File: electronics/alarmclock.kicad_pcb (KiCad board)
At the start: 2 copper layers, 16 parts, among them J1 SWD, J2 AudioJack2, J3 Conn_02x08_Top_Bottom, J4 SocketTop, J5 SocketBottom, J6 PinheaderTop, J7 PinheaderBottom, SW1 Reset, SW2 Rotary_Encoder_Switch, U1 STM32L011K4T6

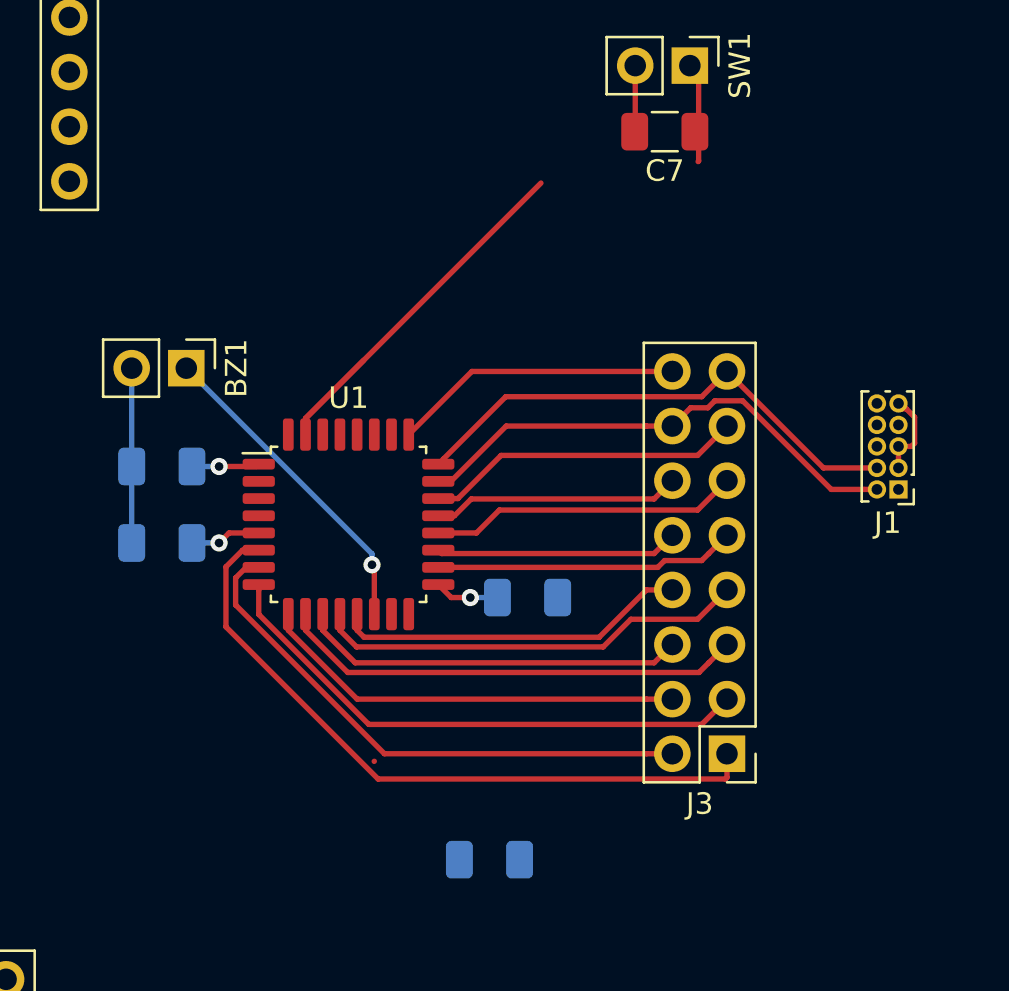
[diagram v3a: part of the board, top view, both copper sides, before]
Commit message: yet another microcontroller switch. added shiftregisters, added battery backup
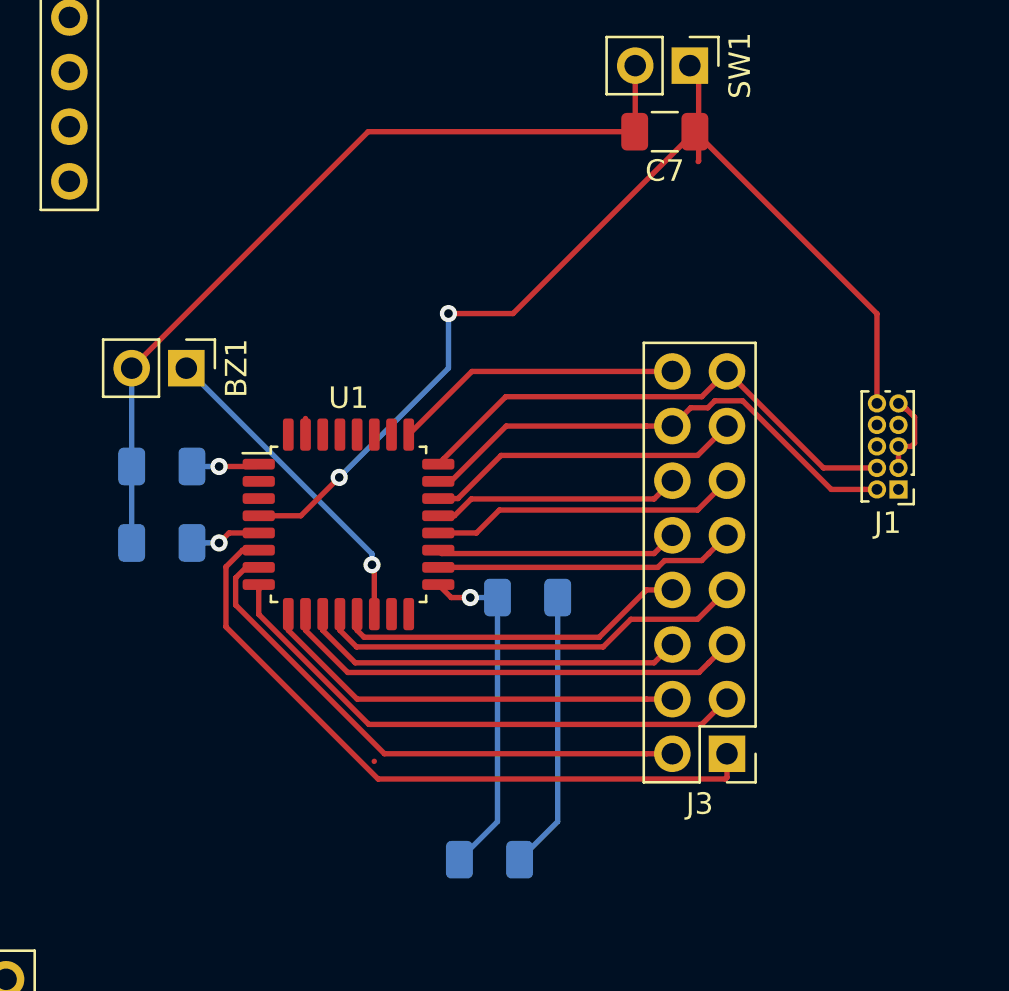
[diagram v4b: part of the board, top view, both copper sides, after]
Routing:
- net NRST: track 4.64 -> 50.0 mm, vias 0 -> 2
- net GND: track 15.3 -> 56.1 mm
- net Switch_Encoder: track 20.1 -> 0.75 mm
- net +3V3: track 9.46 -> 22.4 mm
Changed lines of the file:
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@@
     (thickness 1.6)
     (drawings 0)
-    (tracks 132)
+    (tracks 146)
     (zones 0)
     (modules 16)
@@
       (effects (font (size 1 1) (thickness 0.15)))
     )
-    (fp_text user %R (at 0 8.89 90) (layer F.Fab)
-      (effects (font (size 1 1) (thickness 0.15)))
-    )
     (fp_line (start -1.27 -1.27) (end 0.635 -1.27) (layer F.Fab) (width 0.1))
     (fp_line (start 0.635 -1.27) (end 1.27 -0.635) (layer F.Fab) (width 0.1))
@@
     (fp_line (start 1.75 19.55) (end -1.8 19.55) (layer F.CrtYd) (width 0.05))
     (fp_line (start -1.8 19.55) (end -1.8 -1.8) (layer F.CrtYd) (width 0.05))
+    (fp_text user %R (at 0 8.89 90) (layer F.Fab)
+      (effects (font (size 1 1) (thickness 0.15)))
+    )
     (pad 8 thru_hole oval (at 0 17.78) (size 1.7 1.7) (drill 1) (layers *.Cu *.Mask)
       (net 23 "Net-(J4-Pad8)"))
@@
       (effects (font (size 1 1) (thickness 0.15)))
     )
-    (fp_text user %R (at 0 8.89 90) (layer F.Fab)
-      (effects (font (size 1 1) (thickness 0.15)))
-    )
     (fp_line (start -1.8 19.55) (end -1.8 -1.8) (layer F.CrtYd) (width 0.05))
     (fp_line (start 1.75 19.55) (end -1.8 19.55) (layer F.CrtYd) (width 0.05))
@@
     (fp_line (start 0.635 -1.27) (end 1.27 -0.635) (layer F.Fab) (width 0.1))
     (fp_line (start -1.27 -1.27) (end 0.635 -1.27) (layer F.Fab) (width 0.1))
+    (fp_text user %R (at 0 8.89 90) (layer F.Fab)
+      (effects (font (size 1 1) (thickness 0.15)))
+    )
     (pad 1 thru_hole rect (at 0 0) (size 1.7 1.7) (drill 1) (layers *.Cu *.Mask)
       (net 31 "Net-(J5-Pad1)"))
@@
       (effects (font (size 1 1) (thickness 0.15)))
     )
-    (fp_text user %R (at 0 8.89 90) (layer F.Fab)
-      (effects (font (size 1 1) (thickness 0.15)))
-    )
     (fp_line (start 1.8 -1.8) (end -1.8 -1.8) (layer F.CrtYd) (width 0.05))
     (fp_line (start 1.8 19.55) (end 1.8 -1.8) (layer F.CrtYd) (width 0.05))
@@
     (fp_line (start 1.27 -1.27) (end 1.27 19.05) (layer F.Fab) (width 0.1))
     (fp_line (start -0.635 -1.27) (end 1.27 -1.27) (layer F.Fab) (width 0.1))
+    (fp_text user %R (at 0 8.89 90) (layer F.Fab)
+      (effects (font (size 1 1) (thickness 0.15)))
+    )
     (pad 1 thru_hole rect (at 0 0) (size 1.7 1.7) (drill 1) (layers *.Cu *.Mask)
       (net 30 "Net-(J4-Pad1)"))
@@
       (effects (font (size 1 1) (thickness 0.15)))
     )
-    (fp_text user %R (at 0 8.89 90) (layer F.Fab)
-      (effects (font (size 1 1) (thickness 0.15)))
-    )
     (fp_line (start -0.635 -1.27) (end 1.27 -1.27) (layer F.Fab) (width 0.1))
     (fp_line (start 1.27 -1.27) (end 1.27 19.05) (layer F.Fab) (width 0.1))
@@
     (fp_line (start 1.8 19.55) (end 1.8 -1.8) (layer F.CrtYd) (width 0.05))
     (fp_line (start 1.8 -1.8) (end -1.8 -1.8) (layer F.CrtYd) (width 0.05))
+    (fp_text user %R (at 0 8.89 90) (layer F.Fab)
+      (effects (font (size 1 1) (thickness 0.15)))
+    )
     (pad 8 thru_hole oval (at 0 17.78) (size 1.7 1.7) (drill 1) (layers *.Cu *.Mask)
       (net 38 "Net-(J5-Pad8)"))
@@
   (segment (start 156.9276 79.2924) (end 158.3088 79.2924) (width 0.25) (layer F.Cu) (net 1))
   (segment (start 156.464 79.756) (end 156.9276 79.2924) (width 0.25) (layer F.Cu) (net 1))
+  (segment (start 169.412 92.716) (end 167.64 94.488) (width 0.25) (layer B.Cu) (net 1))
+  (segment (start 169.412 82.296) (end 169.412 92.716) (width 0.25) (layer B.Cu) (net 1))
   (segment (start 188.0616 75.2668) (end 188.0616 76.2668) (width 0.25) (layer F.Cu) (net 2))
   (segment (start 188.811601 75.117839) (end 188.66264 75.2668) (width 0.25) (layer F.Cu) (net 2))
@@
   (segment (start 152.4 76.2) (end 152.4 79.756) (width 0.25) (layer B.Cu) (net 2))
   (segment (start 152.4 71.628) (end 152.4 76.2) (width 0.25) (layer B.Cu) (net 2))
+  (segment (start 163.3982 60.6298) (end 152.4 71.628) (width 0.25) (layer F.Cu) (net 2))
+  (segment (start 175.7934 60.6298) (end 163.3982 60.6298) (width 0.25) (layer F.Cu) (net 2))
+  (segment (start 172.212 92.716) (end 170.44 94.488) (width 0.25) (layer B.Cu) (net 2))
+  (segment (start 172.212 82.296) (end 172.212 92.716) (width 0.25) (layer B.Cu) (net 2))
   (segment (start 178.7682 61.993588) (end 178.741589 62.020199) (width 0.25) (layer F.Cu) (net 3))
   (segment (start 178.7682 60.5282) (end 178.7682 61.993588) (width 0.25) (layer F.Cu) (net 3))
   (segment (start 178.7682 57.9658) (end 178.3588 57.5564) (width 0.25) (layer F.Cu) (net 3))
   (segment (start 178.7682 60.5282) (end 178.7682 57.9658) (width 0.25) (layer F.Cu) (net 3))
+  (segment (start 187.0616 69.098) (end 178.5934 60.6298) (width 0.25) (layer F.Cu) (net 3))
+  (segment (start 187.0616 73.2668) (end 187.0616 69.098) (width 0.25) (layer F.Cu) (net 3))
+  (segment (start 178.5934 60.6298) (end 170.1352 69.088) (width 0.25) (layer F.Cu) (net 3))
+  (via (at 167.132 69.088) (size 0.8) (drill 0.4) (layers F.Cu B.Cu) (net 3))
+  (segment (start 170.1352 69.088) (end 167.132 69.088) (width 0.25) (layer F.Cu) (net 3))
+  (segment (start 167.132 71.628) (end 162.052 76.708) (width 0.25) (layer B.Cu) (net 3))
+  (via (at 162.052 76.708) (size 0.8) (drill 0.4) (layers F.Cu B.Cu) (net 3))
+  (segment (start 167.132 69.088) (end 167.132 71.628) (width 0.25) (layer B.Cu) (net 3))
+  (segment (start 160.2676 78.4924) (end 158.3088 78.4924) (width 0.25) (layer F.Cu) (net 3))
+  (segment (start 162.052 76.708) (end 160.2676 78.4924) (width 0.25) (layer F.Cu) (net 3))
   (segment (start 176.343919 74.3204) (end 177.546 74.3204) (width 0.25) (layer F.Cu) (net 4))
   (segment (start 169.817212 74.3204) (end 176.343919 74.3204) (width 0.25) (layer F.Cu) (net 4))
@@
   (segment (start 163.6838 80.8798) (end 163.576 80.772) (width 0.25) (layer F.Cu) (net 41))
   (segment (start 163.6838 83.0674) (end 163.6838 80.8798) (width 0.25) (layer F.Cu) (net 41))
-  (segment (start 160.4838 73.9674) (end 163.195 71.2562) (width 0.25) (layer F.Cu) (net 48))
   (segment (start 160.4838 74.7174) (end 160.4838 73.9674) (width 0.25) (layer F.Cu) (net 48))
-  (segment (start 160.4838 73.9674) (end 171.4338 63.0174) (width 0.25) (layer F.Cu) (net 48))
 )

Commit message: made most of the pcb
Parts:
- added C10: 1uF, Capacitor_SMD:C_1206_3216Metric, F.Cu at (103.4, 131.9)
- added C11: 1uF, Capacitor_SMD:C_1206_3216Metric, F.Cu at (97.2, 127.1)
- added C5: 100nF, Capacitor_SMD:C_1206_3216Metric, F.Cu at (104.4, 112.9)
- added C6: 100nF, Capacitor_SMD:C_1206_3216Metric, F.Cu at (119.6, 112.9)
- added C8: 12pF, Capacitor_SMD:C_0805_2012Metric, F.Cu at (100.8, 113.2)
- added C9: 0.1uF, Capacitor_SMD:C_1206_3216Metric, F.Cu at (71.4, 105.3)
- added D1: D_Schottky_Small, Diode_SMD:D_1206_3216Metric_Pad1.42x1.75mm_HandSolder, F.Cu at (79.4, 125.6)
- added JP1: SolderJumper_2_Open, Jumper:SolderJumper-2_P1.3mm_Open_TrianglePad1.0x1.5mm, F.Cu at (108.4, 120.5)
- added JP2: SolderJumper_BOOT0, Jumper:SolderJumper-3_P2.0mm_Open_TrianglePad1.0x1.5mm, F.Cu at (108.4, 106.5)
- added Q1: Backpower, Package_TO_SOT_SMD:SOT-323_SC-70_Handsoldering, F.Cu at (112.2, 120.6)
- added R1: R_Small, Resistor_SMD:R_1206_3216Metric, F.Cu at (117.3, 120.7)
- added R10: R_Small, Resistor_SMD:R_1206_3216Metric, B.Cu at (110.3, 54.7)
- added R11: R_Small, Resistor_SMD:R_1206_3216Metric, B.Cu at (112.9, 54.7)
- added R12: R_Small, Resistor_SMD:R_1206_3216Metric, B.Cu at (95.7, 66.1)
- added R17: R_Small, Resistor_SMD:R_1206_3216Metric, B.Cu at (107.2, 67.4)
- added R18: R_Small, Resistor_SMD:R_1206_3216Metric, B.Cu at (110.4, 67.4)
- added R3: R_Small, Resistor_SMD:R_1206_3216Metric, B.Cu at (93.2, 54.5)
- added R4: R_Small, Resistor_SMD:R_1206_3216Metric, B.Cu at (95.7, 54.5)
- added R8: R_Small, Resistor_SMD:R_1206_3216Metric, B.Cu at (107.8, 54.7)
- added R9: R_Small, Resistor_SMD:R_1206_3216Metric, B.Cu at (93.2, 66.1)
- added U2: 74HCT595, Package_SO:TSSOP-16_4.4x5mm_P0.65mm, B.Cu at (84.0, 57.3)
- added U3: 74HCT595, Package_SO:TSSOP-16_4.4x5mm_P0.65mm, B.Cu at (83.3, 68.8)
- added U4: AP2111H-3.3, Package_TO_SOT_SMD:SOT-223-3_TabPin2, F.Cu at (103.3, 125.0)
- added Y1: 24MHz, Crystal:Crystal_SMD_SeikoEpson_MC146-4Pin_6.7x1.5mm_HandSoldering, F.Cu at (97.8, 111.4)
- C1: moved to F.Cu
- C4: value 100nF -> 4.7uF; moved to F.Cu
- C7: value 0.1uF -> 12pF; footprint Capacitor_SMD:C_1206_3216Metric -> Capacitor_SMD:C_0805_2012Metric
- J1: value SWD -> Conn_01x02; footprint Connector_PinHeader_1.00mm:PinHeader_2x05_P1.00mm_Vertical -> Connector_PinHeader_2.54mm:PinHeader_1x02_P2.54mm_Vertical
- J2: value AudioJack2 -> SWD; footprint Connector_PinHeader_2.54mm:PinHeader_1x02_P2.54mm_Vertical -> Connector_PinHeader_1.00mm:PinHeader_2x05_P1.00mm_Vertical
- J3: value Conn_02x08_Top_Bottom -> SocketTop; footprint Connector_PinHeader_2.54mm:PinHeader_2x08_P2.54mm_Vertical -> Connector_PinSocket_2.54mm:PinSocket_1x08_P2.54mm_Vertical
- J4: value SocketTop -> SocketBottem
- J5: value SocketBottom -> Conn_01x02; footprint Connector_PinSocket_2.54mm:PinSocket_1x08_P2.54mm_Vertical -> Connector_PinHeader_2.54mm:PinHeader_1x02_P2.54mm_Vertical
- J6: value PinheaderTop -> Conn_01x05; footprint Connector_PinHeader_2.54mm:PinHeader_1x08_P2.54mm_Vertical -> Connector_PinHeader_2.54mm:PinHeader_1x05_P2.54mm_Vertical; moved to B.Cu
- J7: value PinheaderBottom -> Conn_01x05; footprint Connector_PinHeader_2.54mm:PinHeader_1x08_P2.54mm_Vertical -> Connector_PinHeader_2.54mm:PinHeader_1x05_P2.54mm_Vertical
- SW1: value Reset -> RotaryEncoder_Switch; footprint Connector_PinHeader_2.54mm:PinHeader_1x02_P2.54mm_Vertical -> Rotary_Encoder:RotaryEncoder_Bourns_Horizontal_PEC09-2xxxF-Nxxxx
- SW2: value Rotary_Encoder_Switch -> Reset; footprint Connector_PinHeader_2.54mm:PinHeader_1x05_P2.54mm_Vertical -> Connector_PinHeader_2.54mm:PinHeader_1x02_P2.54mm_Vertical
- U1: value STM32L011K4T6 -> STM32L031F6P6; footprint Package_QFP:LQFP-32_7x7mm_P0.8mm -> Package_SO:TSSOP-20_4.4x6.5mm_P0.65mm
- moved J5 184.7 mm to (70.3, 118.0), turned to 90 degrees
- moved J7 177.8 mm to (88.1, 111.6)
- moved J6 151.9 mm to (71.6, 65.9)
- moved J4 139.7 mm to (93.2, 61.9), turned to 90 degrees
- moved J1 103.8 mm to (102.3, 135.7), turned to 90 degrees
- moved C1 101.1 mm to (76.7, 53.4), turned to 90 degrees
- moved SW1 100.1 mm to (85.6, 95.1), turned to 0 degrees
- moved SW2 97.9 mm to (70.3, 110.3), turned to 90 degrees
- moved J3 95.6 mm to (93.2, 49.7), turned to 90 degrees
- moved BZ1 94.7 mm to (70.3, 114.2), turned to 90 degrees
- moved C7 90.6 mm to (100.8, 109.4), turned to -90 degrees
- moved C3 75.8 mm to (82.8, 53.2), turned to 0 degrees
- moved C2 72.8 mm to (82.0, 64.6), turned to 0 degrees
- moved U1 60.7 mm to (112.2, 112.9)
- moved C4 44.8 mm to (132.3, 105.3)
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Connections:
- BZ1 pad 1: Alarm -> GND
- BZ1 pad 2: GND -> Alarm
- C1 pad 1: +3V3 -> +5V
- C2 pad 1: +3V3 -> +5V
- C3 pad 1: +3V3 -> +5V
- C4 pad 1: +3V3 -> +BATT
- C7 pad 1: NRST -> GND
- C7 pad 2: GND -> OSC_IN
- J1 pad 1: +3V3 -> GND
- J1 pad 2: SWDIO -> +5V
- J2 pad 1: (no net) -> +3V3
- J2 pad 2: (no net) -> SWDIO
- J3 pad 1: LED_0 -> Net-(J3-Pin_1)
- J3 pad 2: LED_1 -> Net-(J3-Pin_2)
- J3 pad 3: LED_2 -> Net-(J3-Pin_3)
- J3 pad 4: LED_3 -> Net-(J3-Pin_4)
- J3 pad 5: LED_4 -> Net-(J3-Pin_5)
- J3 pad 6: LED_5 -> Net-(J3-Pin_6)
- J3 pad 7: LED_6 -> Net-(J3-Pin_7)
- J3 pad 8: LED_7 -> Net-(J3-Pin_8)
- J4 pad 1: Net-(J4-Pad1) -> Net-(J4-Pin_1)
- J4 pad 2: Net-(J4-Pad2) -> Net-(J4-Pin_2)
- J4 pad 3: Net-(J4-Pad3) -> Net-(J4-Pin_3)
- J4 pad 4: Net-(J4-Pad4) -> Net-(J4-Pin_4)
- J4 pad 5: Net-(J4-Pad5) -> Net-(J4-Pin_5)
- J4 pad 6: Net-(J4-Pad6) -> Net-(J4-Pin_6)
- J4 pad 7: Net-(J4-Pad7) -> Net-(J4-Pin_7)
- J4 pad 8: Net-(J4-Pad8) -> Net-(J4-Pin_8)
- J5 pad 1: Net-(J5-Pad1) -> GND
- J5 pad 2: Net-(J5-Pad2) -> Mute_button
- J6 pad 1: Net-(J4-Pad1) -> GND
- J6 pad 2: Net-(J4-Pad2) -> SRCLK_DIS
- J6 pad 3: Net-(J4-Pad3) -> RCLK_DIS
- J6 pad 4: Net-(J4-Pad4) -> SHIFT_IN_DIS
- J6 pad 5: Net-(J4-Pad5) -> +5V
- J7 pad 1: Net-(J5-Pad1) -> GND
- J7 pad 2: Net-(J5-Pad2) -> SRCLK
- J7 pad 3: Net-(J5-Pad3) -> RCLK
- J7 pad 4: Net-(J5-Pad4) -> SHIFT_IN
- J7 pad 5: Net-(J5-Pad5) -> +5V
- SW2 pad 1: (no net) -> GND
- SW2 pad 2: (no net) -> NRST
- U1 pad 1: +3V3 -> BOOT0
- U1 pad 10: LED_4 -> SHIFT_IN
- U1 pad 11: LED_5 -> Rotary_B
- U1 pad 12: LED_6 -> Switch_Encoder
- U1 pad 13: LED_7 -> Rotary_A
- U1 pad 14: Alarm -> +3.3V
- U1 pad 15: Mute_button -> GND
- U1 pad 16: GND -> +BATT
- U1 pad 17: +3V3 -> Vbat_enable
- U1 pad 18: LED_8 -> unconnected-(U1-PA10-Pad18)
- U1 pad 19: LED_9 -> SWDIO
- U1 pad 2: Net-(U1-Pad2) -> OSC_IN
- U1 pad 20: LED_10 -> SWCLK
- U1 pad 3: Net-(U1-Pad3) -> OSC_OUT
- U1 pad 5: +3V3 -> +BATT
- U1 pad 6: LED_0 -> Alarm
- U1 pad 7: LED_1 -> Mute_button
- U1 pad 8: LED_2 -> SRCLK
- U1 pad 9: LED_3 -> RCLK
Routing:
- net +5V: track 0.00 -> 45.6 mm, vias 0 -> 4
- net NRST: track 50.0 -> 11.5 mm, vias 2 -> 0
- net LED_0: track 32.0 -> 0.00 mm
- net Net-(U2-QH): track 0.00 -> 27.2 mm
- net RCLK_DIS: track 0.00 -> 26.1 mm, vias 0 -> 2
- net LED_2: track 25.8 -> 0.00 mm
- net LED_1: track 25.7 -> 0.00 mm
- net GND: track 56.1 -> 30.7 mm, vias 0 -> 5
- net +BATT: track 0.00 -> 25.4 mm
- net +3.3V: track 0.00 -> 25.3 mm
- net Net-(U3-QH): track 0.00 -> 25.0 mm
- net Net-(U2-QG): track 0.00 -> 24.4 mm
- net SRCLK_DIS: track 0.00 -> 23.2 mm
- net Net-(J4-Pin_6): track 0.00 -> 23.1 mm
- net +3V3: track 22.4 -> 0.00 mm, vias 3 -> 0
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- added copper zone on B.Cu, net GND
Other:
- board outline added: 100.3 x 102.9 mm
- net class Default removed

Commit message: finilised for review
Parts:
- removed SW1: RotaryEncoder_Switch, Rotary_Encoder:RotaryEncoder_Bourns_Horizontal_PEC09-2xxxF-Nxxxx
- added BT1: 2450 coin, Battery:BatteryHolder_ComfortableElectronic_CH273-2450_1x2450, F.Cu at (92.8, 132.7)
- added J8: RotaryEncoder, Connector_PinHeader_2.54mm:PinHeader_1x05_P2.54mm_Vertical, F.Cu at (84.5, 93.3)
- C1: moved to B.Cu
- moved J2 57.1 mm to (68.4, 84.9), turned to -90 degrees
- moved C4 56.9 mm to (77.0, 118.7), turned to 180 degrees
- moved C6 56.2 mm to (71.0, 84.9), turned to 90 degrees
- moved JP2 48.6 mm to (62.2, 91.5), turned to -90 degrees
- moved U1 46.1 mm to (71.0, 92.3), turned to 90 degrees
- moved C1 38.8 mm to (96.5, 86.8)
- moved R10 38.7 mm to (130.5, 87.7)
- moved R12 38.7 mm to (115.9, 99.1)
- moved R18 38.7 mm to (130.6, 100.4)
- moved R4 38.7 mm to (115.9, 87.5)
- moved U3 38.7 mm to (103.5, 101.8)
- moved C2 38.7 mm to (102.1, 97.6)
- moved C3 38.7 mm to (103.0, 86.2)
- moved J3 38.7 mm to (113.3, 82.7)
- moved J6 38.7 mm to (91.8, 98.9)
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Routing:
- net +BATT: track 25.4 -> 84.7 mm, vias 0 -> 4
- net +5V: track 45.6 -> 90.2 mm
- net +3.3V: track 25.3 -> 64.2 mm
- net Vbat_enable: track 12.2 -> 42.2 mm, vias 0 -> 2
- net Mute_button: track 0.00 -> 22.6 mm
- net NRST: track 11.5 -> 32.9 mm
- net Rotary_A: track 0.00 -> 15.6 mm
- net Switch_Encoder: track 0.00 -> 13.9 mm
- net Alarm: track 0.00 -> 13.9 mm
- net SRCLK: track 0.00 -> 13.6 mm
- net Rotary_B: track 0.00 -> 11.7 mm
- net RCLK: track 0.00 -> 10.8 mm
- net SHIFT_IN: track 0.00 -> 7.98 mm
- net GND: track 30.7 -> 25.4 mm, vias 5 -> 6
- net Net-(BT1-+): track 0.00 -> 4.49 mm
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- added copper zone on F.Cu, net GND
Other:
- board size 100.3 x 102.9 mm -> 100.3 x 69.9 mm
